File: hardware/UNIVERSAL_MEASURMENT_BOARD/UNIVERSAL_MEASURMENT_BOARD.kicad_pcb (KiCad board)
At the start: 6 copper layers, 75 x 95 mm, 198 parts, among them J1 2606-1110_010-000, J2 2606-1110_010-000, J3 2606-1110_010-000, J4 2606-1110_010-000, J5 Strain Relief, J6 Strain Relief, J7 FTSH-107-01-L-D-K, J8 Strain Relief, J9 Strain Relief, U1 ADS8863IDGS, U10 LT3471EDD#PBF, U11 L7812ABD2T-TR, U12 ISL21010CFH330Z-TK, U13 L78L15ACD13TR, U14 TPS54202HDDCR, U15 L79L15ACD13TR, U16 ADM3057EBRWZ, U2 STM32G484RET3, U3 PGA280AIPW, U4 CD4097BM, U5 UA78M33CDCYRG3, U6 TPS54202HDDCR, U7 UA78M33CDCYRG3, U8 L7805ABD2T-TR, U9 ISL21010CFH315Z-TK, Y1 ATX-H11-F-16.000MHz-G100-T

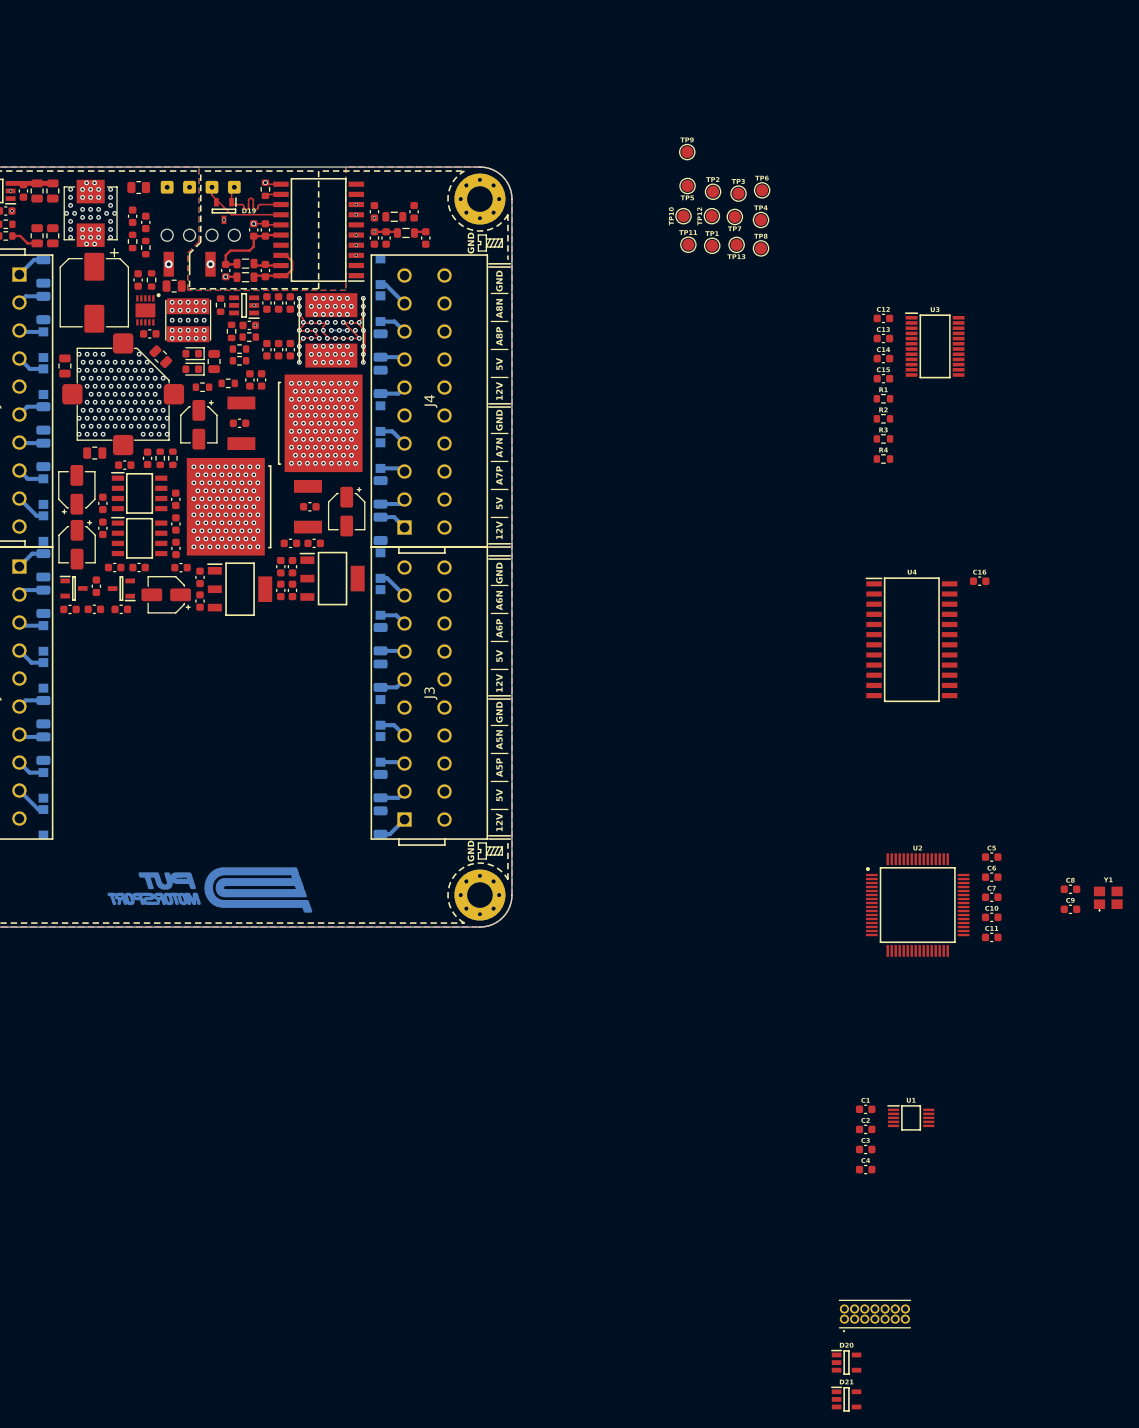
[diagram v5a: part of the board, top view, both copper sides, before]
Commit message: Done board layout:
- Add MCU, PGA, and ADC

- Add programming port and TVSs

- Add additional thermal vias to LDOs
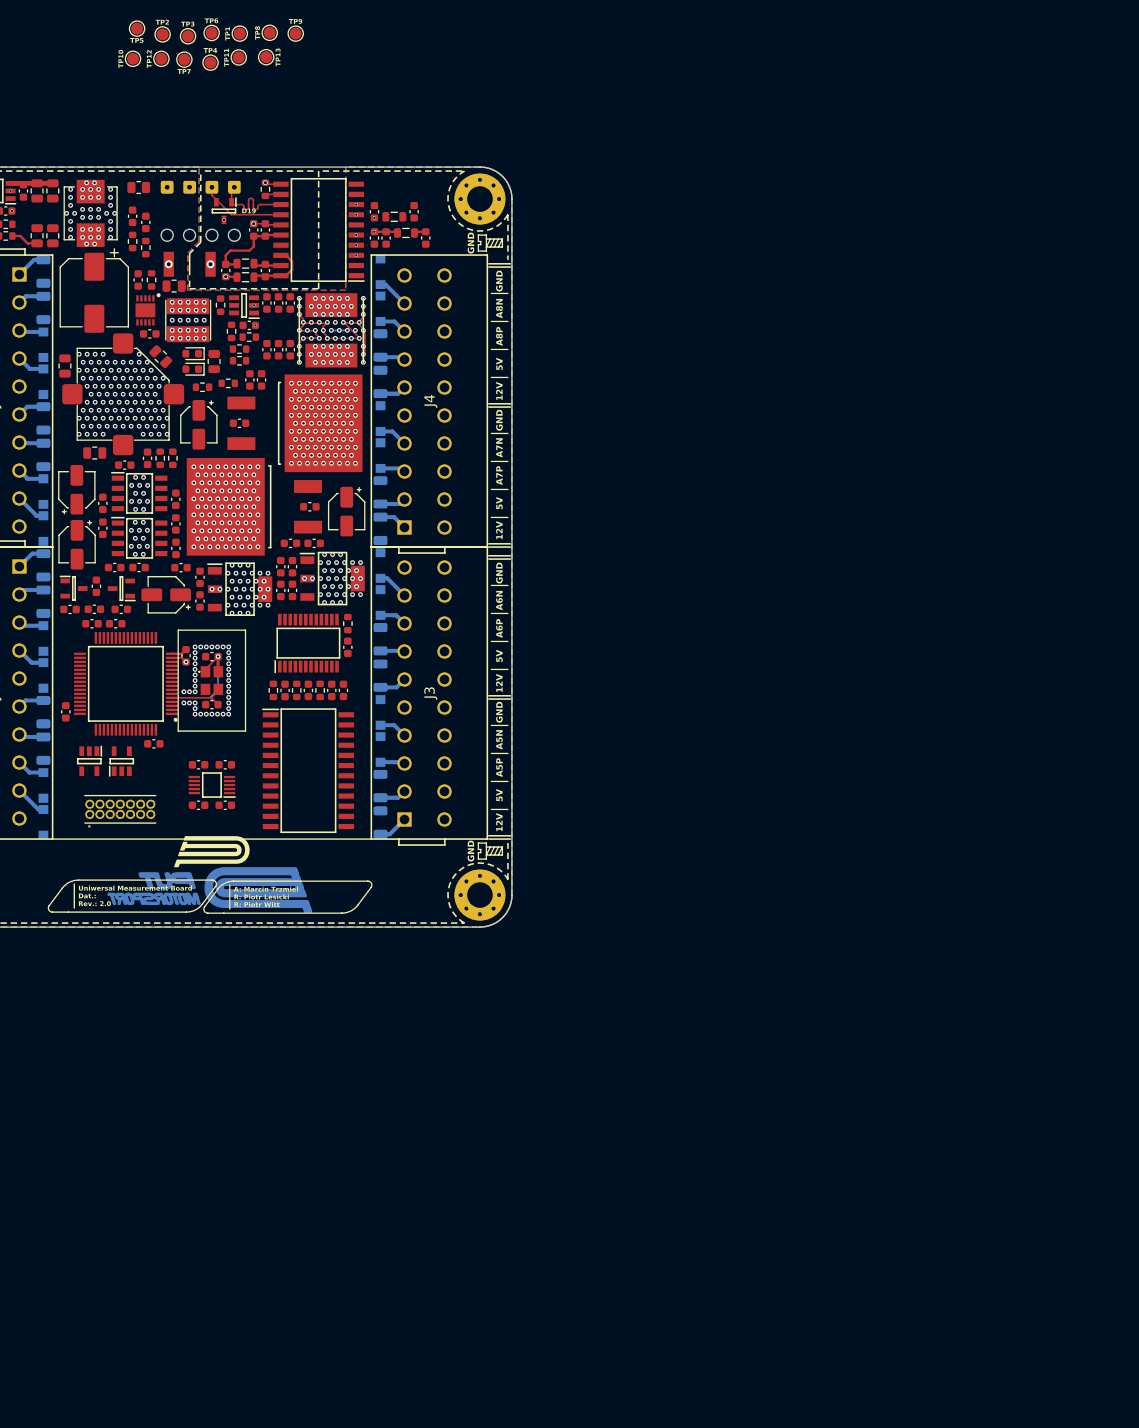
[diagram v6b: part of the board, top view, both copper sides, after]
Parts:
- moved D21 123.8 mm to (59.2, 117.7), turned to -90 degrees
- moved C7 118.0 mm to (56.3, 111.5), turned to 90 degrees
- moved D20 117.7 mm to (63.3, 117.7), turned to 90 degrees
- moved C6 116.8 mm to (59.6, 100.5)
- moved Y1 115.3 mm to (74.5, 107.6), turned to -90 degrees
- moved J7 113.5 mm to (63.1, 123.7)
- moved C5 113.3 mm to (62.5, 100.5)
- moved C8 111.2 mm to (74.5, 104.6), turned to 180 degrees
- moved C9 110.3 mm to (74.5, 110.6), turned to 180 degrees
- moved C10 107.0 mm to (67.3, 115.5), turned to 180 degrees
- moved C11 106.7 mm to (71.3, 104.5), turned to -90 degrees
- moved U2 102.8 mm to (63.8, 108.0), turned to 180 degrees
- moved U1 96.8 mm to (74.5, 120.6), turned to 180 degrees
- moved C2 95.0 mm to (72.9, 118.1), turned to 180 degrees
- moved C3 93.4 mm to (76.2, 118.1)
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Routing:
- net +3V3: track 0.00 -> 12.0 mm, vias 0 -> 1
- net /mcu & adc/HSE: track 0.00 -> 7.56 mm
- net GND: track 33.5 -> 35.5 mm, vias 359 -> 495
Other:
- board text added: "A: Marcin Trzmiel R: Piotr Lesicki R: Piotr Witt"
- board text added: "STACKUP: 1. SIGNAL / POWER 2. GND 3. SIGNAL / POWER 4. SIGNAL / POWER 5. GND 6. SIGNAL / POWER"
- board text added: "U7"
- board text added: "Uniwersal Measurement Board Dat.: Rev.: 2.0"
- board text removed: "STACKUP: 1. SIGNAL / POWER 2. GND 3. SIGNAL / POWER ON PS 4. SIGNAL / POWER ON PS 5. GND 6. SIGNAL / POWER"
